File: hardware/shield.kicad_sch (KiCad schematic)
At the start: 12 parts, among them P1 Power, P10 CONN_01X01, P2 Analog, P3 GPIO, P4 GPIO, P5 GPIO, P6 CONN_01X01, P7 CONN_01X01, P8 CONN_01X01, P9 CONN_01X01

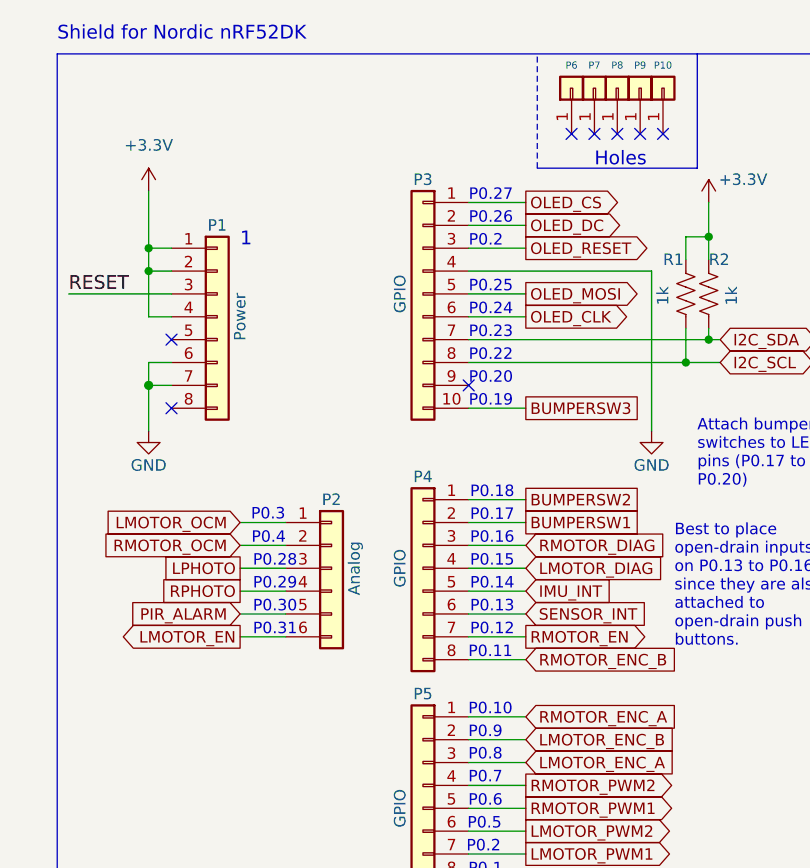
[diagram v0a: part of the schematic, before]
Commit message: First revision of the shield PCB
I have a few more tweaks that I would like to make before I send this
off to be manufactured. I ended up going with a 4 layer board as it has
signal wires going all over the place since I was a bit contrained with
part placement by most of the Arduino signal pins being on the right
side of the board and wanting to place connectors on the side closest
to the part to which they connect.
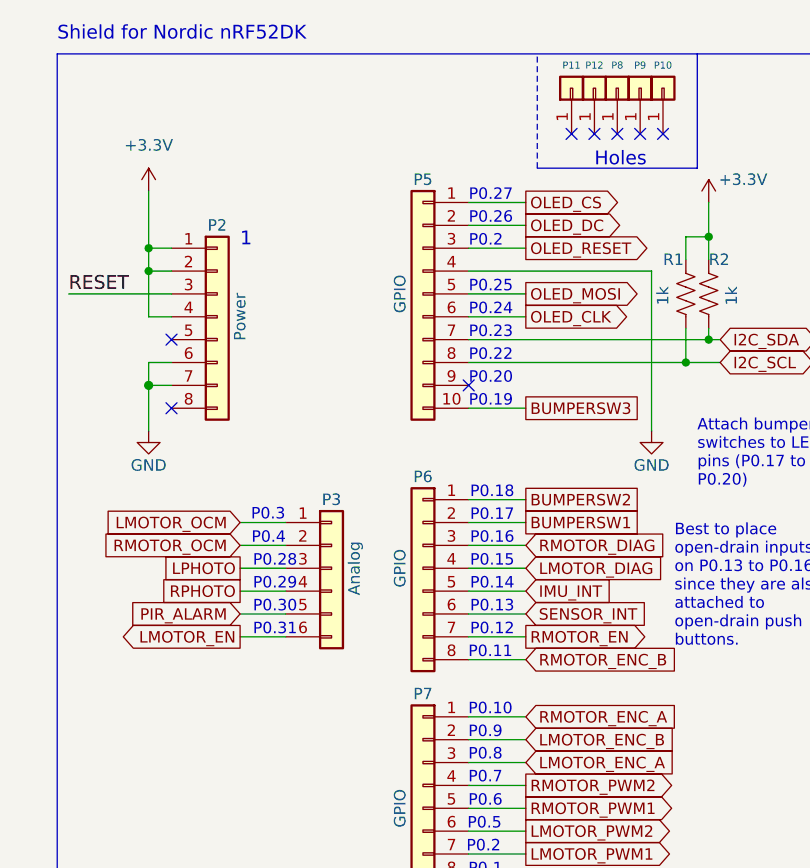
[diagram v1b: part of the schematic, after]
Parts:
- renumbered P6 to P11, P7 to P12, P1 to P2, P2 to P3, P3 to P5, P4 to P6, P5 to P7
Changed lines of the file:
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@@
   (symbol (lib_id "Connector_Generic:Conn_01x01") (at 153.67 33.02 90) (unit 1)
     (in_bom yes) (on_board yes)
-    (property "Reference" "P6" (id 0) (at 153.67 30.48 90)
+    (property "Reference" "P11" (id 0) (at 153.67 30.48 90)
       (effects (font (size 0.7874 0.7874)))
     )
@@
   (symbol (lib_id "Connector_Generic:Conn_01x01") (at 156.21 33.02 90) (unit 1)
     (in_bom yes) (on_board yes)
-    (property "Reference" "P7" (id 0) (at 156.21 30.48 90)
+    (property "Reference" "P12" (id 0) (at 156.21 30.48 90)
       (effects (font (size 0.7874 0.7874)))
     )
@@
   (symbol (lib_id "Connector_Generic:Conn_01x08") (at 114.3 58.42 0) (unit 1)
     (in_bom yes) (on_board yes)
-    (property "Reference" "P1" (id 0) (at 114.3 48.26 0))
+    (property "Reference" "P2" (id 0) (at 114.3 48.26 0))
     (property "Value" "Power" (id 1) (at 116.84 58.42 90))
     (property "Footprint" "Socket_Arduino_Mega:Socket_Strip_Arduino_1x08" (id 2) (at 114.3 58.42 0)
@@
   (symbol (lib_id "Connector_Generic:Conn_01x10") (at 137.16 55.88 0) (mirror y) (unit 1)
     (in_bom yes) (on_board yes)
-    (property "Reference" "P3" (id 0) (at 137.16 43.18 0))
+    (property "Reference" "P5" (id 0) (at 137.16 43.18 0))
     (property "Value" "GPIO" (id 1) (at 134.62 55.88 90))
     (property "Footprint" "Socket_Arduino_Mega:Socket_Strip_Arduino_1x10" (id 2) (at 137.16 55.88 0)
@@
   (symbol (lib_id "Connector_Generic:Conn_01x06") (at 127 86.36 0) (unit 1)
     (in_bom yes) (on_board yes)
-    (property "Reference" "P2" (id 0) (at 127 78.74 0))
+    (property "Reference" "P3" (id 0) (at 127 78.74 0))
     (property "Value" "Analog" (id 1) (at 129.54 86.36 90))
     (property "Footprint" "Connector_PinHeader_2.54mm:PinHeader_1x06_P2.54mm_Vertical" (id 2) (at 127 86.36 0)
@@
   (symbol (lib_id "Connector_Generic:Conn_01x08") (at 137.16 86.36 0) (mirror y) (unit 1)
     (in_bom yes) (on_board yes)
-    (property "Reference" "P4" (id 0) (at 137.16 76.2 0))
+    (property "Reference" "P6" (id 0) (at 137.16 76.2 0))
     (property "Value" "GPIO" (id 1) (at 134.62 86.36 90))
     (property "Footprint" "Socket_Arduino_Mega:Socket_Strip_Arduino_1x08" (id 2) (at 137.16 86.36 0)
@@
   (symbol (lib_id "Connector_Generic:Conn_01x09") (at 137.16 113.03 0) (mirror y) (unit 1)
     (in_bom yes) (on_board yes)
-    (property "Reference" "P5" (id 0) (at 137.16 100.33 0))
+    (property "Reference" "P7" (id 0) (at 137.16 100.33 0))
     (property "Value" "GPIO" (id 1) (at 134.62 113.03 90))
     (property "Footprint" "Connector_PinHeader_2.54mm:PinHeader_1x09_P2.54mm_Vertical" (id 2) (at 137.16 113.03 0)
@@
       (reference "#FLG05") (unit 1) (value "PWR_FLAG") (footprint "")
     )
+    (path "/4c28e167-2325-477c-a275-ed3fbfcf1a06/2a2a609a-4a66-42eb-95c9-22185e654daa"
+      (reference "#FLG06") (unit 1) (value "PWR_FLAG") (footprint "")
+    )
     (path "/c6d3c3d8-232a-4757-8648-b1d250ada124"
       (reference "#PWR01") (unit 1) (value "+3.3V") (footprint "")
@@
       (reference "#PWR025") (unit 1) (value "GND") (footprint "")
     )
-    (path "/fa8f6b07-7d40-4224-a9dc-a3ae06b76dce/6bf9fa91-6352-4e77-820c-84d19daf0056"
-      (reference "#PWR026") (unit 1) (value "+3.3V") (footprint "")
-    )
-    (path "/fa8f6b07-7d40-4224-a9dc-a3ae06b76dce/cefe2a86-f212-417c-bded-15a3daf68b83"
-      (reference "#PWR027") (unit 1) (value "GND") (footprint "")
+    (path "/4c28e167-2325-477c-a275-ed3fbfcf1a06/a2054aec-7067-45fc-ad56-8be7ad00d51e"
+      (reference "#PWR026") (unit 1) (value "VCC") (footprint "")
     )
     (path "/fa8f6b07-7d40-4224-a9dc-a3ae06b76dce/684f8cc4-5df0-4d23-ab6d-9327b7150341"
@@
       (reference "J11") (unit 1) (value "Front Center Distance Sensor") (footprint "Connector_PinSocket_2.54mm:PinSocket_1x07_P2.54mm_Vertical")
     )
-    (path "/fa8f6b07-7d40-4224-a9dc-a3ae06b76dce/fce34feb-a679-4207-bfd2-6ee7a8e91af8"
-      (reference "J12") (unit 1) (value "Back Center Distance Sensor") (footprint "Connector_PinSocket_2.54mm:PinSocket_1x07_P2.54mm_Vertical")
-    )
     (path "/fa8f6b07-7d40-4224-a9dc-a3ae06b76dce/94517954-83cb-4fc7-9baa-5ebc7d4b74eb"
-      (reference "J13") (unit 1) (value "Bumper Switch 1") (footprint "Connector_PinSocket_2.54mm:PinSocket_1x02_P2.54mm_Vertical")
+      (reference "J13") (unit 1) (value "Bumper Switch 1") (footprint "Connector_PinSocket_2.54mm:PinSocket_1x02_P2.54mm_Horizontal")
     )
     (path "/fa8f6b07-7d40-4224-a9dc-a3ae06b76dce/72556355-70a9-4b7d-b310-0fb788bbf3c7"
-      (reference "J14") (unit 1) (value "Bumper Switch 2") (footprint "Connector_PinSocket_2.54mm:PinSocket_1x02_P2.54mm_Vertical")
+      (reference "J14") (unit 1) (value "Bumper Switch 2") (footprint "Connector_PinSocket_2.54mm:PinSocket_1x02_P2.54mm_Horizontal")
     )
     (path "/fa8f6b07-7d40-4224-a9dc-a3ae06b76dce/1d294281-1e4b-49e0-aceb-f1ea3f848d1d"
-      (reference "J15") (unit 1) (value "Bumper Switch 3") (footprint "Connector_PinSocket_2.54mm:PinSocket_1x02_P2.54mm_Vertical")
+      (reference "J15") (unit 1) (value "Bumper Switch 3") (footprint "Connector_PinSocket_2.54mm:PinSocket_1x02_P2.54mm_Horizontal")
     )
     (path "/fa8f6b07-7d40-4224-a9dc-a3ae06b76dce/d3051d8f-5266-489d-9e3d-0145522584e5"
@@
     )
     (path "/fa8f6b07-7d40-4224-a9dc-a3ae06b76dce/a014ebbd-2c2d-471f-a9ea-21ecea81ec81"
-      (reference "J19") (unit 1) (value "Left Cliff Sensor") (footprint "Connector_PinSocket_2.54mm:PinSocket_1x07_P2.54mm_Vertical")
+      (reference "J19") (unit 1) (value "Left Cliff Sensor") (footprint "Connector_PinSocket_2.54mm:PinSocket_1x07_P2.54mm_Horizontal")
     )
     (path "/fa8f6b07-7d40-4224-a9dc-a3ae06b76dce/cbbf99b0-f621-4255-9478-f224af720ca8"
-      (reference "J20") (unit 1) (value "Right Cliff Sensor") (footprint "Connector_PinSocket_2.54mm:PinSocket_1x07_P2.54mm_Vertical")
+      (reference "J20") (unit 1) (value "Right Cliff Sensor") (footprint "Connector_PinSocket_2.54mm:PinSocket_1x07_P2.54mm_Horizontal")
     )
     (path "/fa8f6b07-7d40-4224-a9dc-a3ae06b76dce/84375f8b-a254-4cdf-a053-6e6c22a58f9b"
@@
     )
     (path "/2bb6c136-8f3a-4530-8b08-9c3c632d4195/7385c06f-c56f-4edf-843c-21a50d007fa2"
-      (reference "J26") (unit 1) (value "LeftMotor Conn") (footprint "Connector_PinSocket_2.54mm:PinSocket_1x06_P2.54mm_Vertical")
+      (reference "J26") (unit 1) (value "LeftMotor Conn") (footprint "Connector_PinSocket_2.54mm:PinSocket_1x06_P2.54mm_Horizontal")
     )
     (path "/2bb6c136-8f3a-4530-8b08-9c3c632d4195/2f3ca387-0a81-462f-a184-dfe2120fe907"
-      (reference "J27") (unit 1) (value "RightMotor Conn") (footprint "Connector_PinSocket_2.54mm:PinSocket_1x06_P2.54mm_Vertical")
+      (reference "J27") (unit 1) (value "RightMotor Conn") (footprint "Connector_PinSocket_2.54mm:PinSocket_1x06_P2.54mm_Horizontal")
     )
     (path "/00000000-0000-0000-0000-000056d71773"
-      (reference "P1") (unit 1) (value "Power") (footprint "Socket_Arduino_Mega:Socket_Strip_Arduino_1x08")
+      (reference "P2") (unit 1) (value "Power") (footprint "Socket_Arduino_Mega:Socket_Strip_Arduino_1x08")
     )
     (path "/00000000-0000-0000-0000-000056d72f1c"
-      (reference "P2") (unit 1) (value "Analog") (footprint "Connector_PinHeader_2.54mm:PinHeader_1x06_P2.54mm_Vertical")
+      (reference "P3") (unit 1) (value "Analog") (footprint "Connector_PinHeader_2.54mm:PinHeader_1x06_P2.54mm_Vertical")
     )
     (path "/00000000-0000-0000-0000-000056d72368"
-      (reference "P3") (unit 1) (value "GPIO") (footprint "Socket_Arduino_Mega:Socket_Strip_Arduino_1x10")
+      (reference "P5") (unit 1) (value "GPIO") (footprint "Socket_Arduino_Mega:Socket_Strip_Arduino_1x10")
     )
     (path "/00000000-0000-0000-0000-000056d734d0"
-      (reference "P4") (unit 1) (value "GPIO") (footprint "Socket_Arduino_Mega:Socket_Strip_Arduino_1x08")
+      (reference "P6") (unit 1) (value "GPIO") (footprint "Socket_Arduino_Mega:Socket_Strip_Arduino_1x08")
     )
     (path "/00000000-0000-0000-0000-000056d73f2c"
-      (reference "P5") (unit 1) (value "GPIO") (footprint "Connector_PinHeader_2.54mm:PinHeader_1x09_P2.54mm_Vertical")
-    )
-    (path "/00000000-0000-0000-0000-000056d70b71"
-      (reference "P6") (unit 1) (value "CONN_01X01") (footprint "Socket_Arduino_Mega:Arduino_1pin")
-    )
-    (path "/00000000-0000-0000-0000-000056d70c9b"
-      (reference "P7") (unit 1) (value "CONN_01X01") (footprint "Socket_Arduino_Mega:Arduino_1pin")
+      (reference "P7") (unit 1) (value "GPIO") (footprint "Connector_PinHeader_2.54mm:PinHeader_1x09_P2.54mm_Vertical")
     )
     (path "/00000000-0000-0000-0000-000056d70ce6"
@@
       (reference "P10") (unit 1) (value "CONN_01X01") (footprint "Socket_Arduino_Mega:Arduino_1pin")
     )
+    (path "/00000000-0000-0000-0000-000056d70b71"
+      (reference "P11") (unit 1) (value "CONN_01X01") (footprint "Socket_Arduino_Mega:Arduino_1pin")
+    )
+    (path "/00000000-0000-0000-0000-000056d70c9b"
+      (reference "P12") (unit 1) (value "CONN_01X01") (footprint "Socket_Arduino_Mega:Arduino_1pin")
+    )
     (path "/1f8d776f-9c79-4c6f-806d-c75493f77acb"

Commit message: Cleanup PCB layout
* Made the board outline a bit smaller.
* Added the 3D .step files for all of the parts that I could find. This
  was all the parts except for the IMU from Adafruit.
* Fixed an issue where I had the back distance sensors facing in the
  wrong direction.
* Added CC BY-SA licensing info for the KiCad design files.
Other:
- title: (none) -> RugRover Shield
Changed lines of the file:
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@@
   (paper "A")
   (title_block
+    (title "RugRover Shield")
     (date "2022-03-29")
     (rev "0.1")
+    (comment 1 "CC BY-SA 4.0")
   )
   (junction (at 106.68 53.34) (diameter 0) (color 0 0 0 0)
